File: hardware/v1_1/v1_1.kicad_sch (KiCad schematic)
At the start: 74 parts, among them J1 AUDIO IN, J2 MIDI OUT, J3 MIDI IN, J4 MIDI THRU, J5 OUTPUT R, J6 OUTPUT L - MONO, J7 EXP 2, J8 EXP 1, J9 Batt In, SW1 RotaryEncoder_Switch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

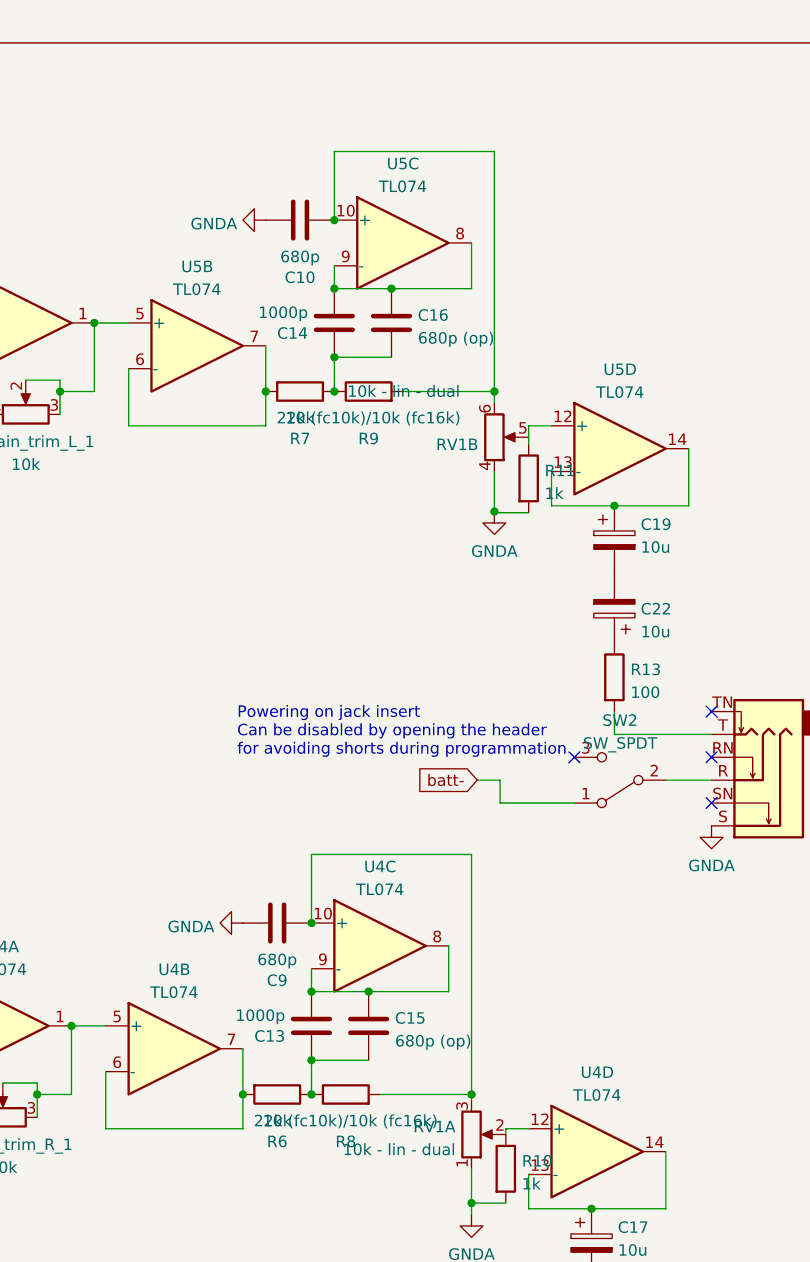
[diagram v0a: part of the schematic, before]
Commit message: Corrected output filter
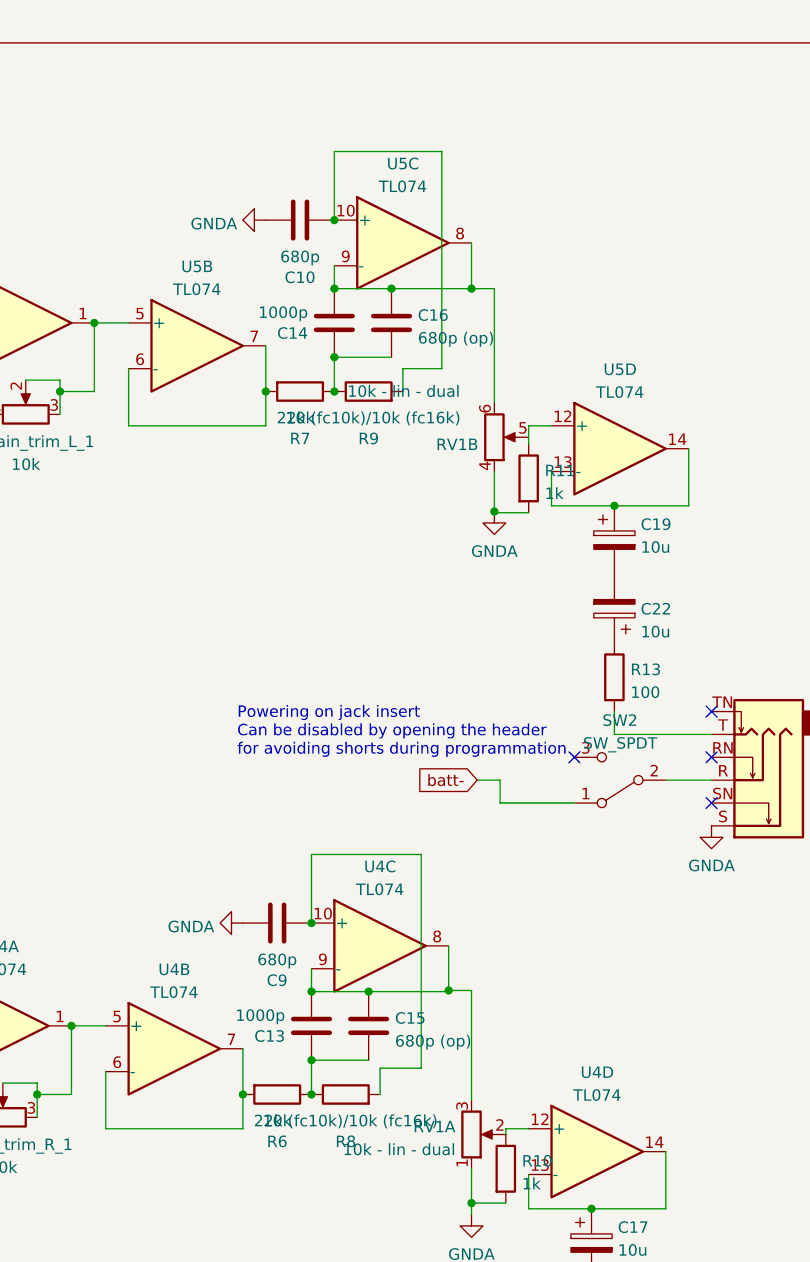
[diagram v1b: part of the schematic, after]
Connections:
- net at C9.2, R8.2, U4.10 (+): no longer RV1.3
- net at C10.2, R9.2, U5.10 (+): no longer RV1.6
- net at C14.2, C16.1, U5.8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: now also RV1.6
- net at C13.2, C15.1, U4.8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: now also RV1.3
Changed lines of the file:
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@@
   (junction (at 362.585 20.32) (diameter 0) (color 0 0 0 0)
   )
+  (junction (at 441.96 35.56) (diameter 0) (color 0 0 0 0)
+  )
   (junction (at 441.96 137.16) (diameter 0) (color 0 0 0 0)
   )
@@
   (junction (at 136.525 30.48) (diameter 0) (color 0 0 0 0)
   )
+  (junction (at 439.42 113.538) (diameter 0) (color 0 0 0 0)
+  )
   (junction (at 148.59 30.48) (diameter 0) (color 0 0 0 0)
   )
@@
   (junction (at 354.965 20.32) (diameter 0) (color 0 0 0 0)
   )
-  (junction (at 441.96 125.095) (diameter 0) (color 0 0 0 0)
-  )
   (junction (at 430.53 113.665) (diameter 0) (color 0 0 0 0)
   )
   (junction (at 455.295 137.795) (diameter 0) (color 0 0 0 0)
-  )
-  (junction (at 444.5 46.99) (diameter 0) (color 0 0 0 0)
   )
   (junction (at 186.69 22.86) (diameter 0) (color 0 0 0 0)
@@
     (stroke (width 0) (type default) (color 0 0 0 0))
   )
-  (wire (pts (xy 441.96 125.73) (xy 441.96 125.095))
-    (stroke (width 0) (type default) (color 0 0 0 0))
-  )
   (wire (pts (xy 58.42 36.83) (xy 58.42 82.55))
     (stroke (width 0) (type default) (color 0 0 0 0))
@@
     (stroke (width 0) (type default) (color 0 0 0 0))
   )
-  (wire (pts (xy 444.5 20.32) (xy 426.72 20.32))
+  (wire (pts (xy 438.658 20.32) (xy 426.72 20.32))
     (stroke (width 0) (type default) (color 0 0 0 0))
   )
@@
     (stroke (width 0) (type default) (color 0 0 0 0))
   )
+  (wire (pts (xy 441.96 35.56) (xy 444.5 35.56))
+    (stroke (width 0) (type default) (color 0 0 0 0))
+  )
   (wire (pts (xy 142.875 59.69) (xy 60.96 59.69))
     (stroke (width 0) (type default) (color 0 0 0 0))
@@
     (stroke (width 0) (type default) (color 0 0 0 0))
   )
-  (wire (pts (xy 444.5 20.32) (xy 444.5 46.99))
+  (wire (pts (xy 438.658 20.32) (xy 438.658 44.45))
     (stroke (width 0) (type default) (color 0 0 0 0))
   )
@@
     (stroke (width 0) (type default) (color 0 0 0 0))
   )
+  (wire (pts (xy 444.5 35.56) (xy 444.5 48.26))
+    (stroke (width 0) (type default) (color 0 0 0 0))
+  )
   (wire (pts (xy 225.425 130.175) (xy 225.425 128.905))
     (stroke (width 0) (type default) (color 0 0 0 0))
@@
     (stroke (width 0) (type default) (color 0 0 0 0))
   )
+  (wire (pts (xy 434.34 44.45) (xy 434.34 46.99))
+    (stroke (width 0) (type default) (color 0 0 0 0))
+  )
   (wire (pts (xy 392.43 45.72) (xy 396.24 45.72))
     (stroke (width 0) (type default) (color 0 0 0 0))
@@
     (stroke (width 0) (type default) (color 0 0 0 0))
   )
-  (wire (pts (xy 441.96 98.425) (xy 424.18 98.425))
+  (wire (pts (xy 436.372 98.425) (xy 424.18 98.425))
     (stroke (width 0) (type default) (color 0 0 0 0))
   )
@@
     (stroke (width 0) (type default) (color 0 0 0 0))
   )
-  (wire (pts (xy 431.8 125.095) (xy 441.96 125.095))
+  (wire (pts (xy 431.8 122.174) (xy 436.372 122.174))
     (stroke (width 0) (type default) (color 0 0 0 0))
   )
@@
     (stroke (width 0) (type default) (color 0 0 0 0))
   )
+  (wire (pts (xy 439.42 113.538) (xy 441.96 113.538))
+    (stroke (width 0) (type default) (color 0 0 0 0))
+  )
   (polyline (pts (xy 81.915 141.605) (xy 81.915 158.75))
     (stroke (width 0) (type default) (color 0 0 0 0))
@@
     (stroke (width 0) (type default) (color 0 0 0 0))
   )
+  (wire (pts (xy 441.96 30.48) (xy 441.96 35.56))
+    (stroke (width 0) (type default) (color 0 0 0 0))
+  )
   (wire (pts (xy 107.95 92.71) (xy 107.95 87.63))
     (stroke (width 0) (type default) (color 0 0 0 0))
@@
     (stroke (width 0) (type default) (color 0 0 0 0))
   )
+  (wire (pts (xy 439.42 113.538) (xy 439.42 108.585))
+    (stroke (width 0) (type default) (color 0 0 0 0))
+  )
   (polyline (pts (xy 81.915 158.75) (xy 59.69 158.75))
     (stroke (width 0) (type default) (color 0 0 0 0))
@@
     (stroke (width 0) (type default) (color 0 0 0 0))
   )
+  (wire (pts (xy 441.96 113.538) (xy 441.96 125.73))
+    (stroke (width 0) (type default) (color 0 0 0 0))
+  )
   (polyline (pts (xy 108.585 170.815) (xy 108.585 192.405))
     (stroke (width 0) (type default) (color 0 0 0 0))
@@
     (stroke (width 0) (type default) (color 0 0 0 0))
   )
-  (wire (pts (xy 439.42 113.665) (xy 439.42 108.585))
+  (wire (pts (xy 439.42 113.665) (xy 439.42 113.538))
     (stroke (width 0) (type default) (color 0 0 0 0))
   )
@@
     (stroke (width 0) (type default) (color 0 0 0 0))
   )
+  (wire (pts (xy 431.8 122.174) (xy 431.8 125.095))
+    (stroke (width 0) (type default) (color 0 0 0 0))
+  )
   (wire (pts (xy 393.7 123.825) (xy 393.7 125.095))
     (stroke (width 0) (type default) (color 0 0 0 0))
@@
     (stroke (width 0) (type default) (color 0 0 0 0))
   )
-  (wire (pts (xy 441.96 35.56) (xy 441.96 30.48))
-    (stroke (width 0) (type default) (color 0 0 0 0))
-  )
   (wire (pts (xy 72.39 41.91) (xy 55.88 41.91))
     (stroke (width 0) (type default) (color 0 0 0 0))
   )
-  (wire (pts (xy 444.5 48.26) (xy 444.5 46.99))
-    (stroke (width 0) (type default) (color 0 0 0 0))
-  )
   (wire (pts (xy 457.835 82.55) (xy 457.835 85.09))
     (stroke (width 0) (type default) (color 0 0 0 0))
@@
     (stroke (width 0) (type default) (color 0 0 0 0))
   )
-  (wire (pts (xy 441.96 98.425) (xy 441.96 125.095))
+  (wire (pts (xy 436.372 98.425) (xy 436.372 122.174))
     (stroke (width 0) (type default) (color 0 0 0 0))
   )
@@
     (stroke (width 0) (type default) (color 0 0 0 0))
   )
-  (wire (pts (xy 434.34 46.99) (xy 444.5 46.99))
-    (stroke (width 0) (type default) (color 0 0 0 0))
-  )
+  (wire (pts (xy 434.34 44.45) (xy 438.658 44.45))
+    (stroke (width 0) (type default) (color 0 0 0 0))
+  )

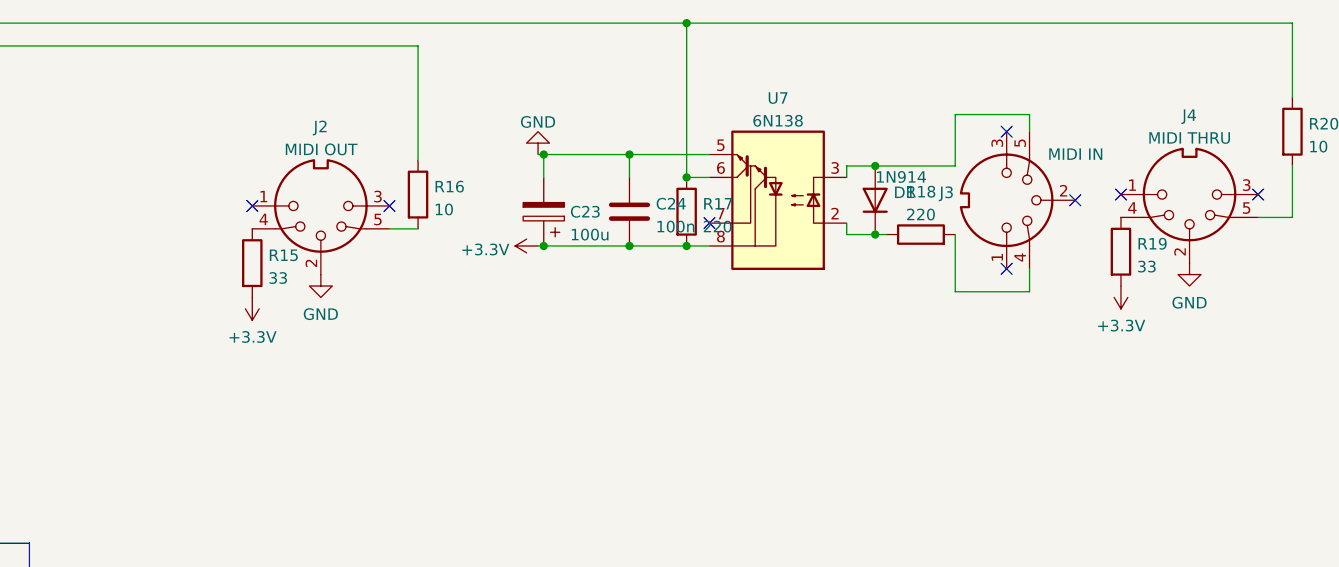
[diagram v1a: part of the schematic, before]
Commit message: Corrected power net, 3V3 is not 3.3V
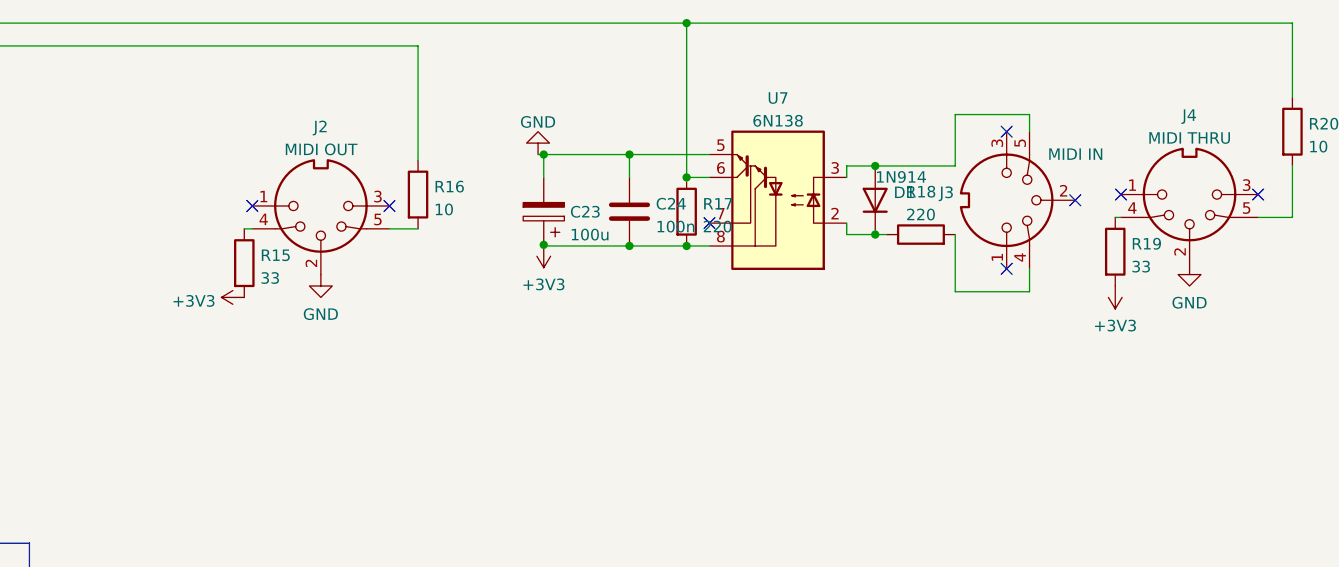
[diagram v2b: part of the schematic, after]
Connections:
- net +3V3: now also R15.2, R19.2
- net +3.3V: no longer names the net of C23.1, C24.2, R17.2, U7.8 (VCC)
- net +3.3V: no longer R15.2, R19.2
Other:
- moved on the sheet: R15, R19
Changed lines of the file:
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@@
   (junction (at 444.5 60.325) (diameter 0) (color 0 0 0 0)
   )
+  (junction (at 191.77 137.668) (diameter 0) (color 0 0 0 0)
+  )
   (junction (at 457.835 59.69) (diameter 0) (color 0 0 0 0)
   )
@@
   (junction (at 148.59 15.24) (diameter 0) (color 0 0 0 0)
   )
-  (junction (at 191.77 137.795) (diameter 0) (color 0 0 0 0)
-  )
   (junction (at 201.295 127.635) (diameter 0) (color 0 0 0 0)
   )
@@
     (stroke (width 0) (type default) (color 0 0 0 0))
   )
+  (wire (pts (xy 255.27 134.62) (xy 255.905 134.62))
+    (stroke (width 0) (type default) (color 0 0 0 0))
+  )
   (wire (pts (xy 40.005 150.495) (xy 31.115 150.495))
     (stroke (width 0) (type default) (color 0 0 0 0))
@@
     (stroke (width 0) (type default) (color 0 0 0 0))
   )
-  (wire (pts (xy 191.135 137.795) (xy 191.77 137.795))
-    (stroke (width 0) (type default) (color 0 0 0 0))
-  )
   (wire (pts (xy 431.8 122.174) (xy 431.8 125.095))
     (stroke (width 0) (type default) (color 0 0 0 0))
@@
     (stroke (width 0) (type default) (color 0 0 0 0))
   )
+  (wire (pts (xy 158.496 135.89) (xy 159.385 135.89))
+    (stroke (width 0) (type default) (color 0 0 0 0))
+  )
   (wire (pts (xy 457.835 82.55) (xy 457.835 85.09))
     (stroke (width 0) (type default) (color 0 0 0 0))
@@
     (pin "2")
   )
-  (symbol (lib_id "Device:R") (at 255.905 138.43 0) (unit 1)
+  (symbol (lib_id "Device:R") (at 255.27 138.43 0) (unit 1)
     (in_bom yes) (on_board yes) (fields_autoplaced)
-    (property "Reference" "R19" (id 0) (at 257.683 137.5953 0)
+    (property "Reference" "R19" (id 0) (at 257.048 137.5953 0)
       (effects (font (size 1.27 1.27)) (justify left))
     )
-    (property "Value" "33" (id 1) (at 257.683 140.1322 0)
+    (property "Value" "33" (id 1) (at 257.048 140.1322 0)
       (effects (font (size 1.27 1.27)) (justify left))
     )
-    (property "Footprint" "Resistor_THT:R_Axial_DIN0207_L6.3mm_D2.5mm_P7.62mm_Horizontal" (id 2) (at 254.127 138.43 90)
+    (property "Footprint" "Resistor_THT:R_Axial_DIN0207_L6.3mm_D2.5mm_P7.62mm_Horizontal" (id 2) (at 253.492 138.43 90)
       (effects (font (size 1.27 1.27)) hide)
     )
-    (property "Datasheet" "~" (id 3) (at 255.905 138.43 0)
+    (property "Datasheet" "~" (id 3) (at 255.27 138.43 0)
       (effects (font (size 1.27 1.27)) hide)
     )
@@
     (pin "2")
   )
+  (symbol (lib_id "power:+3V3") (at 191.77 137.668 180) (unit 1)
+    (in_bom yes) (on_board yes) (fields_autoplaced)
+    (property "Reference" "#PWR?" (id 0) (at 191.77 133.858 0)
+      (effects (font (size 1.27 1.27)) hide)
+    )
+    (property "Value" "+3V3" (id 1) (at 191.77 142.1114 0))
+    (property "Footprint" "" (id 2) (at 191.77 137.668 0)
+      (effects (font (size 1.27 1.27)) hide)
+    )
+    (property "Datasheet" "" (id 3) (at 191.77 137.668 0)
+      (effects (font (size 1.27 1.27)) hide)
+    )
+    (pin "1")
+  )
   (symbol (lib_id "Device:C") (at 163.195 22.86 0) (unit 1)
     (in_bom yes) (on_board yes) (fields_autoplaced)
@@
     (pin "1")
   )
+  (symbol (lib_id "power:+3V3") (at 158.496 143.51 90) (unit 1)
+    (in_bom yes) (on_board yes) (fields_autoplaced)
+    (property "Reference" "#PWR?" (id 0) (at 162.306 143.51 0)
+      (effects (font (size 1.27 1.27)) hide)
+    )
+    (property "Value" "+3V3" (id 1) (at 155.321 143.9438 90)
+      (effects (font (size 1.27 1.27)) (justify left))
+    )
+    (property "Footprint" "" (id 2) (at 158.496 143.51 0)
+      (effects (font (size 1.27 1.27)) hide)
+    )
+    (property "Datasheet" "" (id 3) (at 158.496 143.51 0)
+      (effects (font (size 1.27 1.27)) hide)
+    )
+    (pin "1")
+  )
   (symbol (lib_id "Connector:Conn_01x02_Female") (at 249.555 26.035 0) (unit 1)
     (in_bom yes) (on_board yes) (fields_autoplaced)
@@
     (pin "TN")
   )
+  (symbol (lib_id "power:+3V3") (at 255.27 142.24 180) (unit 1)
+    (in_bom yes) (on_board yes) (fields_autoplaced)
+    (property "Reference" "#PWR?" (id 0) (at 255.27 138.43 0)
+      (effects (font (size 1.27 1.27)) hide)
+    )
+    (property "Value" "+3V3" (id 1) (at 255.27 146.6834 0))
+    (property "Footprint" "" (id 2) (at 255.27 142.24 0)
+      (effects (font (size 1.27 1.27)) hide)
+    )
+    (property "Datasheet" "" (id 3) (at 255.27 142.24 0)
+      (effects (font (size 1.27 1.27)) hide)
+    )
+    (pin "1")
+  )
   (symbol (lib_id "power:GNDA") (at 186.69 22.86 270) (unit 1)
     (in_bom yes) (on_board yes) (fields_autoplaced)
@@
     )
   )
-  (symbol (lib_id "power:+3.3V") (at 191.135 137.795 90) (unit 1)
-    (in_bom yes) (on_board yes) (fields_autoplaced)
-    (property "Reference" "#PWR022" (id 0) (at 194.945 137.795 0)
-      (effects (font (size 1.27 1.27)) hide)
-    )
-    (property "Value" "+3.3V" (id 1) (at 187.96 138.2288 90)
-      (effects (font (size 1.27 1.27)) (justify left))
-    )
-    (property "Footprint" "" (id 2) (at 191.135 137.795 0)
-      (effects (font (size 1.27 1.27)) hide)
-    )
-    (property "Datasheet" "" (id 3) (at 191.135 137.795 0)
-      (effects (font (size 1.27 1.27)) hide)
-    )
-    (pin "1")
-  )
   (symbol (lib_id "Device:C") (at 422.91 27.94 90) (unit 1)
     (in_bom yes) (on_board yes)
@@
     (pin "1")
   )
-  (symbol (lib_id "Device:R") (at 159.385 139.7 0) (unit 1)
+  (symbol (lib_id "Device:R") (at 158.496 139.7 0) (unit 1)
     (in_bom yes) (on_board yes) (fields_autoplaced)
-    (property "Reference" "R15" (id 0) (at 161.163 138.8653 0)
+    (property "Reference" "R15" (id 0) (at 160.274 138.8653 0)
       (effects (font (size 1.27 1.27)) (justify left))
     )
-    (property "Value" "33" (id 1) (at 161.163 141.4022 0)
+    (property "Value" "33" (id 1) (at 160.274 141.4022 0)
       (effects (font (size 1.27 1.27)) (justify left))
     )
-    (property "Footprint" "Resistor_THT:R_Axial_DIN0207_L6.3mm_D2.5mm_P7.62mm_Horizontal" (id 2) (at 157.607 139.7 90)
+    (property "Footprint" "Resistor_THT:R_Axial_DIN0207_L6.3mm_D2.5mm_P7.62mm_Horizontal" (id 2) (at 156.718 139.7 90)
       (effects (font (size 1.27 1.27)) hide)
     )
-    (property "Datasheet" "~" (id 3) (at 159.385 139.7 0)
+    (property "Datasheet" "~" (id 3) (at 158.496 139.7 0)
       (effects (font (size 1.27 1.27)) hide)
     )
@@
     (pin "2")
   )
-  (symbol (lib_id "power:+3.3V") (at 255.905 142.24 180) (unit 1)
-    (in_bom yes) (on_board yes) (fields_autoplaced)
-    (property "Reference" "#PWR023" (id 0) (at 255.905 138.43 0)
-      (effects (font (size 1.27 1.27)) hide)
-    )
-    (property "Value" "+3.3V" (id 1) (at 255.905 146.6834 0))
-    (property "Footprint" "" (id 2) (at 255.905 142.24 0)
-      (effects (font (size 1.27 1.27)) hide)
-    )
-    (property "Datasheet" "" (id 3) (at 255.905 142.24 0)
-      (effects (font (size 1.27 1.27)) hide)
-    )
-    (pin "1")
-  )
   (symbol (lib_id "Device:D") (at 228.6 132.715 90) (unit 1)
     (in_bom yes) (on_board yes)
@@
     (pin "2")
   )
-  (symbol (lib_id "power:+3.3V") (at 159.385 143.51 180) (unit 1)
-    (in_bom yes) (on_board yes) (fields_autoplaced)
-    (property "Reference" "#PWR019" (id 0) (at 159.385 139.7 0)
-      (effects (font (size 1.27 1.27)) hide)
-    )
-    (property "Value" "+3.3V" (id 1) (at 159.385 147.9534 0))
-    (property "Footprint" "" (id 2) (at 159.385 143.51 0)
-      (effects (font (size 1.27 1.27)) hide)
-    )
-    (property "Datasheet" "" (id 3) (at 159.385 143.51 0)
-      (effects (font (size 1.27 1.27)) hide)
-    )
-    (pin "1")
-  )
   (symbol (lib_id "Amplifier_Operational:TL074") (at 431.8 108.585 0) (unit 3)
     (in_bom yes) (on_board yes) (fields_autoplaced)
@@
       (reference "#PWR018") (unit 1) (value "GNDA") (footprint "")
     )
-    (path "/e968dafd-9141-4e3a-adbe-aa72159de6f8"
-      (reference "#PWR019") (unit 1) (value "+3.3V") (footprint "")
-    )
     (path "/fdcfb224-cc11-4f86-9571-7184d7105c24"
       (reference "#PWR020") (unit 1) (value "GND") (footprint "")
@@
       (reference "#PWR021") (unit 1) (value "GND") (footprint "")
     )
-    (path "/83c9b0dd-ae05-4797-9bad-7cb6bf17d901"
-      (reference "#PWR022") (unit 1) (value "+3.3V") (footprint "")
-    )
-    (path "/e3afcb94-6e4a-4780-b008-6893cbbff4db"
-      (reference "#PWR023") (unit 1) (value "+3.3V") (footprint "")
-    )
     (path "/31363469-ed38-47a9-aa43-76f2cc04b139"
       (reference "#PWR024") (unit 1) (value "GND") (footprint "")
@@
       (reference "#PWR0101") (unit 1) (value "GNDA") (footprint "")
     )
+    (path "/34e9ba1d-9178-4dc1-867f-3a0028b2bbb7"
+      (reference "#PWR?") (unit 1) (value "+3V3") (footprint "")
+    )
+    (path "/3d46ad0b-44e7-4b4b-a79a-644f08d4b023"
+      (reference "#PWR?") (unit 1) (value "+3V3") (footprint "")
+    )
+    (path "/6e25aba8-84dd-432e-bc26-a2faeb582ed8"
+      (reference "#PWR?") (unit 1) (value "+3V3") (footprint "")
+    )
     (path "/81d99bdb-ec53-465a-b291-2af811b9ccbb"
